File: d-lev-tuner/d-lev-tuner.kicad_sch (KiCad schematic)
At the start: 20 parts, among them J1 S6B-PH-SM4-TB, U1 STP08CP05, U2 STP08CP05, U3 STP08CP05, U5 AP2112K-3.3

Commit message: finished routing tuner
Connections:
- net +5V: now also J1.6 (Pin_6); no longer J1.1 (Pin_1)
- net CLK: now also J1.5 (Pin_5); no longer J1.2 (Pin_2)
- net GND: now also J1.1 (Pin_1); no longer J1.6 (Pin_6)
- net LE: now also J1.3 (Pin_3); no longer J1.4 (Pin_4)
- net OE: now also J1.2 (Pin_2); no longer J1.5 (Pin_5)
- net SDI: now also J1.4 (Pin_4); no longer J1.3 (Pin_3)
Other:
- moved on the sheet: J1
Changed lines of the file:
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@@
   )
   (no_connect (at 170.18 118.11))
-  (no_connect (at 79.248 73.406))
+  (no_connect (at 79.248 50.546))
   (wire (pts (xy 91.948 150.241) (xy 91.948 145.161))
     (stroke (width 0) (type default))
@@
     )
   )
-  (symbol (lib_id "assorted:Conn_01x06_MountingPin") (at 79.248 60.706 0) (mirror y) (unit 1)
+  (symbol (lib_id "assorted:Conn_01x06_MountingPin") (at 79.248 63.246 180) (unit 1)
     (in_bom yes) (on_board yes) (dnp no)
-    (property "Reference" "J1" (at 77.216 61.6966 0)
+    (property "Reference" "J1" (at 77.216 62.2554 0)
       (effects (font (size 1.27 1.27)) (justify left))
     )
-    (property "Value" "S6B-PH-SM4-TB" (at 77.216 64.2366 0)
+    (property "Value" "S6B-PH-SM4-TB" (at 77.216 59.7154 0)
       (effects (font (size 1.27 1.27)) (justify left))
     )
-    (property "Footprint" "d-lev:JST_PH_S6B-PH-SM4-TB_1x06-1MP_P2.00mm_Horizontal" (at 79.248 60.706 0)
-      (effects (font (size 1.27 1.27)) hide)
-    )
-    (property "Datasheet" "~" (at 79.248 60.706 0)
-      (effects (font (size 1.27 1.27)) hide)
-    )
+    (property "Footprint" "d-lev:JST_PH_S6B-PH-SM4-TB_1x06-1MP_P2.00mm_Horizontal" (at 79.248 63.246 0)
+      (effects (font (size 1.27 1.27)) hide)
+    )
+    (property "Datasheet" "~" (at 79.248 63.246 0)
+      (effects (font (size 1.27 1.27)) hide)
+    )

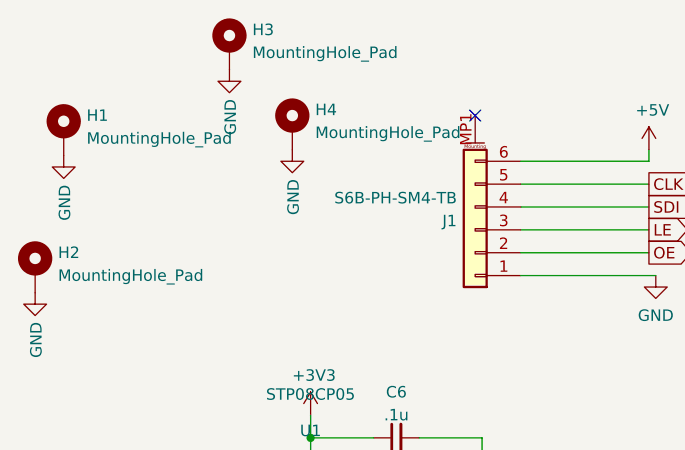
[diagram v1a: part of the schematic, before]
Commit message: tuner: fix led footprints, reroute, place vias artistically
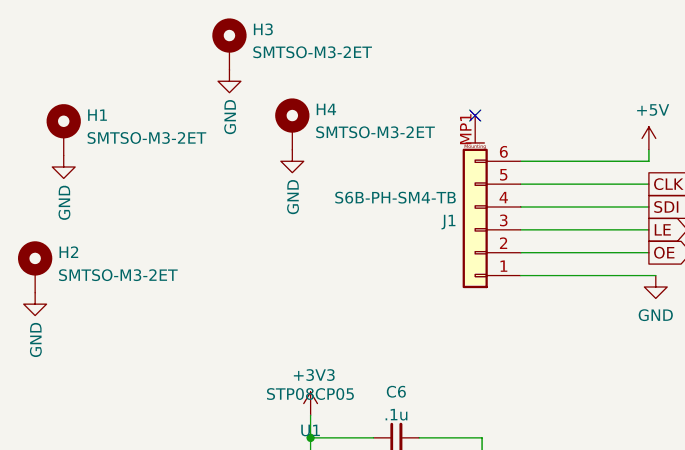
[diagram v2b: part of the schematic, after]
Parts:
- H1, H2, H3, H4: value MountingHole_Pad -> SMTSO-M3-2ET
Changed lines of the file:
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@@
       (effects (font (size 1.27 1.27)) (justify left))
     )
-    (property "Value" "MountingHole_Pad" (at 61.468 52.451 0)
+    (property "Value" "SMTSO-M3-2ET" (at 61.468 52.451 0)
       (effects (font (size 1.27 1.27)) (justify left))
     )
@@
       (effects (font (size 1.27 1.27)) (justify left))
     )
-    (property "Value" "MountingHole_Pad" (at 54.483 43.561 0)
+    (property "Value" "SMTSO-M3-2ET" (at 54.483 43.561 0)
       (effects (font (size 1.27 1.27)) (justify left))
     )
@@
       (effects (font (size 1.27 1.27)) (justify left))
     )
-    (property "Value" "MountingHole_Pad" (at 36.068 53.086 0)
+    (property "Value" "SMTSO-M3-2ET" (at 36.068 53.086 0)
       (effects (font (size 1.27 1.27)) (justify left))
     )
@@
       (effects (font (size 1.27 1.27)) (justify left))
     )
-    (property "Value" "MountingHole_Pad" (at 32.893 68.326 0)
+    (property "Value" "SMTSO-M3-2ET" (at 32.893 68.326 0)
       (effects (font (size 1.27 1.27)) (justify left))
     )

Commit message: Add iBOMs and additional part numbers
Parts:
- C13: MPN (none) -> CL21A106KAYNNNG; Supplier (none) -> Mouser; Supplier URL (none) -> https://www.mouser.com/ProductDetail/187-CL21A106KAYNNNG
- C15, C6, C7, C8: value .1u -> 100n; MPN (none) -> GRM188R71E104KA01D; Notes (none) -> Common; Supplier (none) -> Digi-Key; Supplier URL (none) -> https://www.digikey.com/en/products/detail/murata-electroni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
- H1, H2, H3, H4: MPN (none) -> SMTSO-M3-2ET; Supplier (none) -> Mouser; Supplier Alt (none) -> Aliexpress; Supplier Alt URL (none) -> https://www.aliexpress.us/item/3256803593796853.html; Supplier URL (none) -> https://www.mouser.com/ProductDetail/153-SMTSO-M3-2ET
- J1: MPN (none) -> S6B-PH-SM4-TB; Supplier (none) -> Digi-Key; Supplier Alt (none) -> Aliexpress; Supplier Alt URL (none) -> https://www.aliexpress.us/item/3256805219782364.html; Supplier URL (none) -> https://www.digikey.com/en/products/detail/jst-sales-americ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
- U1, U2, U3: MPN (none) -> 511-STP08CP05TTR; Supplier (none) -> Mouser; Supplier URL (none) -> https://www.mouser.com/ProductDetail/511-STP08CP05TTR
- U5: MPN (none) -> 621-AP2112K-3.3TRG1; Supplier (none) -> Mouser; Supplier URL (none) -> https://www.mouser.com/ProductDetail/621-AP2112K-3.3TRG1
